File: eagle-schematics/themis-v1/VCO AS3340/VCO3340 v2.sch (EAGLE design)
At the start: 47 parts

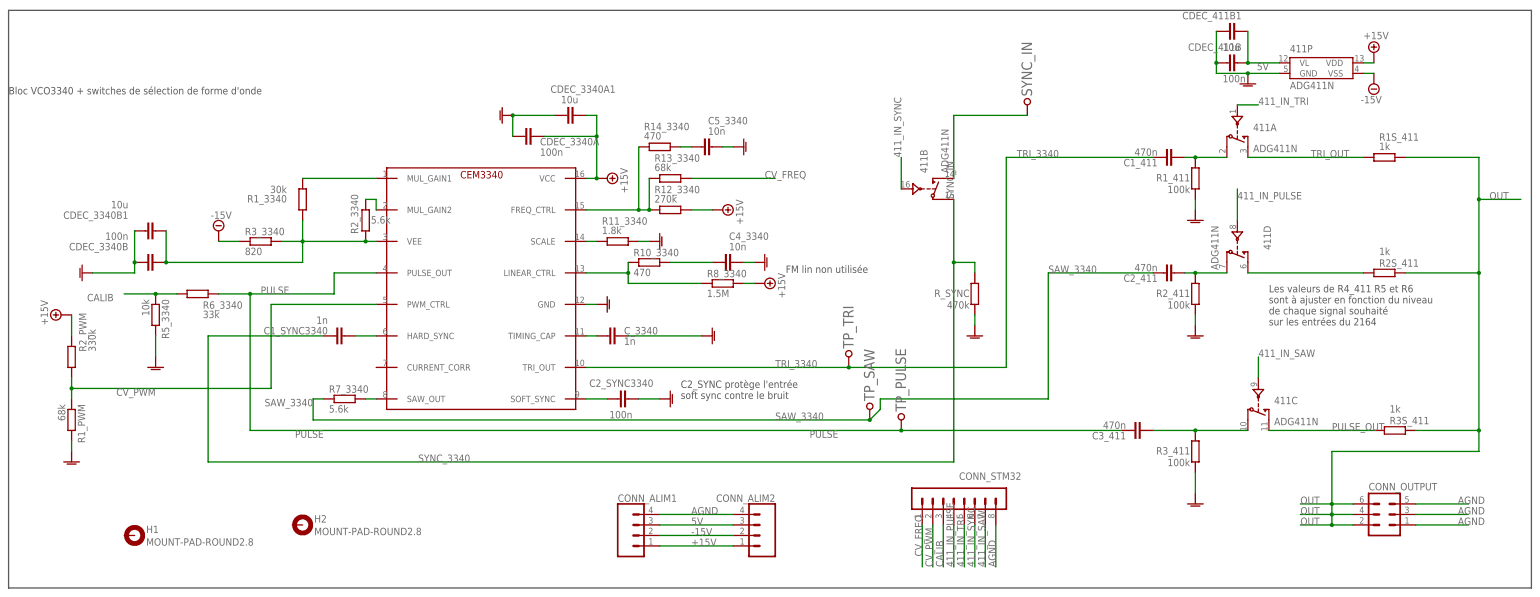
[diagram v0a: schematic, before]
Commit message: New version of DAC board based on AD5391 chip
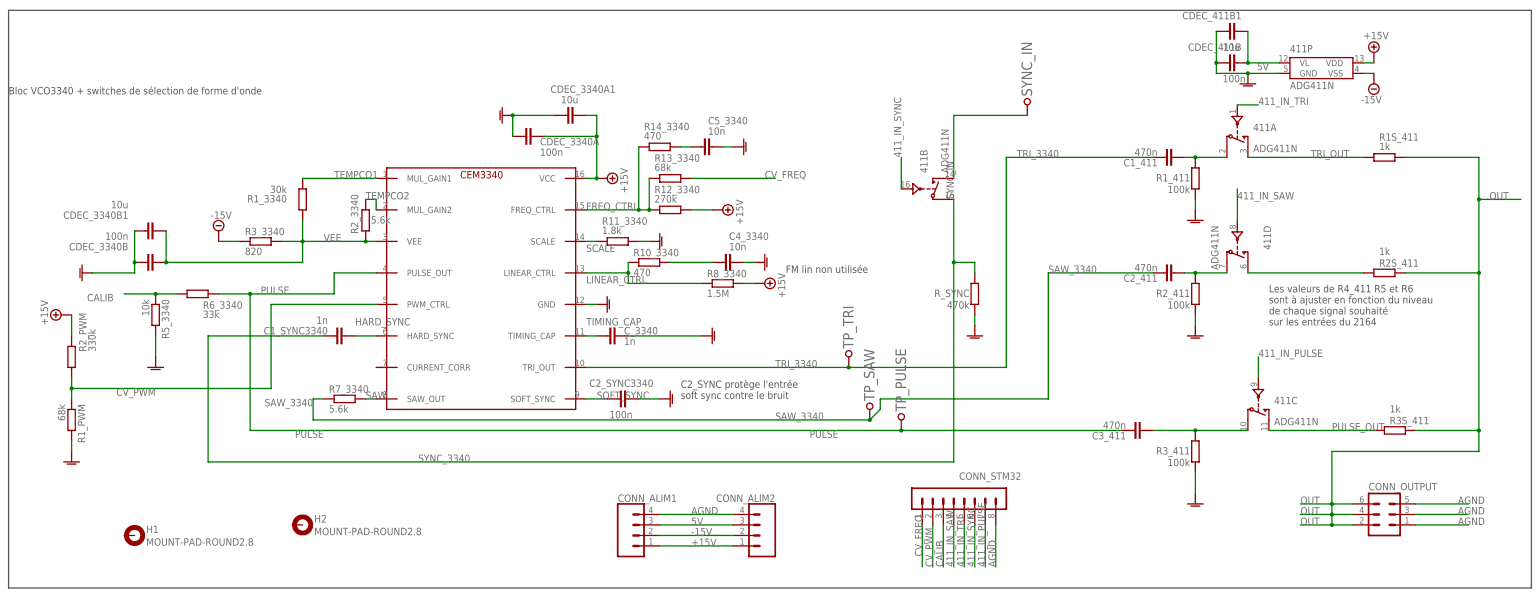
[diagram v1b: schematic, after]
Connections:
- net N$1 renamed SOFT_SYNC
- net N$16 renamed HARD_SYNC
- net N$2 renamed SAW_OUT
- net N$20 renamed TEMPCO1
- net N$23 renamed TEMPCO2
- net N$25 renamed LINEAR_CTRL
- net N$28 renamed SAW
- net N$30 renamed VEE
- net N$40 renamed FREQ_CTRL
- net N$43 renamed SCALE
- net N$46 renamed TIMING_CAP
- net N$49 renamed TRI_IN
- net N$50 renamed SAW_IN
- net N$51 renamed PULSE_IN
- net 411_IN_PULSE: now also 411C.IN, CONN_STM32.7; no longer 411D.IN, CONN_STM32.4
- net 411_IN_SAW: now also 411D.IN, CONN_STM32.4; no longer 411C.IN, CONN_STM32.7
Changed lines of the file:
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@@
 <?xml version="1.0" encoding="utf-8"?>
 <!DOCTYPE eagle SYSTEM "eagle.dtd">
-<eagle version="9.4.2">
+<eagle version="9.5.2">
 <drawing>
 <settings>
@@
 </segment>
 </net>
-<net name="N$20" class="0">
+<net name="TEMPCO1" class="0">
 <segment>
 <pinref part="CEM3340" gate="G$1" pin="MUL_GAIN1"/>
 <pinref part="R1_3340" gate="G$1" pin="1"/>
 <wire x1="-73.66" y1="-78.74" x2="-91.44" y2="-78.74" width="0.1524" layer="91"/>
-</segment>
-</net>
-<net name="N$23" class="0">
+<label x="-83.82" y="-78.74" size="1.778" layer="95"/>
+</segment>
+</net>
+<net name="TEMPCO2" class="0">
 <segment>
 <pinref part="CEM3340" gate="G$1" pin="MUL_GAIN2"/>
@@
 <wire x1="-73.66" y1="-86.36" x2="-73.66" y2="-83.82" width="0.1524" layer="91"/>
 <wire x1="-73.66" y1="-83.82" x2="-76.2" y2="-83.82" width="0.1524" layer="91"/>
-</segment>
-</net>
-<net name="N$28" class="0">
+<label x="-76.2" y="-83.82" size="1.778" layer="95"/>
+</segment>
+</net>
+<net name="SAW" class="0">
 <segment>
 <pinref part="CEM3340" gate="G$1" pin="SAW_OUT"/>
 <pinref part="R7_3340" gate="G$1" pin="2"/>
 <wire x1="-73.66" y1="-132.08" x2="-76.2" y2="-132.08" width="0.1524" layer="91"/>
-</segment>
-</net>
-<net name="N$30" class="0">
+<label x="-76.2" y="-132.08" size="1.778" layer="95"/>
+</segment>
+</net>
+<net name="VEE" class="0">
 <segment>
 <pinref part="CEM3340" gate="G$1" pin="VEE"/>
@@
 <junction x="-124.46" y="-99.06"/>
 <pinref part="CDEC_3340B1" gate="G$1" pin="2"/>
-</segment>
-</net>
-<net name="N$40" class="0">
+<label x="-86.36" y="-93.98" size="1.778" layer="95"/>
+</segment>
+</net>
+<net name="FREQ_CTRL" class="0">
 <segment>
 <pinref part="R14_3340" gate="G$1" pin="1"/>
@@
 <pinref part="R12_3340" gate="G$1" pin="1"/>
 <junction x="-7.62" y="-86.36"/>
+<label x="-22.86" y="-86.36" size="1.778" layer="95"/>
 </segment>
 </net>
@@
 </segment>
 </net>
-<net name="N$43" class="0">
+<net name="SCALE" class="0">
 <segment>
 <pinref part="CEM3340" gate="G$1" pin="SCALE"/>
 <pinref part="R11_3340" gate="G$1" pin="1"/>
 <wire x1="-22.86" y1="-93.98" x2="-20.32" y2="-93.98" width="0.1524" layer="91"/>
+<label x="-22.86" y="-96.52" size="1.778" layer="95"/>
 </segment>
 </net>
@@
 </segment>
 </net>
-<net name="N$46" class="0">
+<net name="TIMING_CAP" class="0">
 <segment>
 <pinref part="CEM3340" gate="G$1" pin="TIMING_CAP"/>
 <pinref part="C_3340" gate="G$1" pin="2"/>
 <wire x1="-22.86" y1="-116.84" x2="-20.32" y2="-116.84" width="0.1524" layer="91"/>
+<label x="-22.86" y="-114.3" size="1.778" layer="95"/>
 </segment>
 </net>
@@
 </segment>
 </net>
-<net name="N$25" class="0">
+<net name="LINEAR_CTRL" class="0">
 <segment>
 <pinref part="CEM3340" gate="G$1" pin="LINEAR_CTRL"/>
@@
 <wire x1="-12.7" y1="-99.06" x2="-12.7" y2="-101.6" width="0.1524" layer="91"/>
 <junction x="-12.7" y="-101.6"/>
+<label x="-22.86" y="-104.14" size="1.778" layer="95"/>
 </segment>
 </net>
@@
 </segment>
 </net>
-<net name="N$49" class="0">
+<net name="TRI_IN" class="0">
 <segment>
 <pinref part="411" gate="A" pin="D"/>
@@
 </segment>
 </net>
-<net name="N$50" class="0">
+<net name="SAW_IN" class="0">
 <segment>
 <pinref part="C2_411" gate="G$1" pin="2"/>
@@
 </segment>
 </net>
-<net name="N$51" class="0">
+<net name="PULSE_IN" class="0">
 <segment>
 <pinref part="411" gate="C" pin="D"/>
@@
 </segment>
 </net>
-<net name="N$1" class="0">
+<net name="SOFT_SYNC" class="0">
 <segment>
 <pinref part="C2_SYNC3340" gate="G$1" pin="2"/>
 <pinref part="CEM3340" gate="G$1" pin="SOFT_SYNC"/>
 <wire x1="-17.78" y1="-132.08" x2="-22.86" y2="-132.08" width="0.1524" layer="91"/>
-</segment>
-</net>
-<net name="N$16" class="0">
+<label x="-20.32" y="-132.08" size="1.778" layer="95"/>
+</segment>
+</net>
+<net name="HARD_SYNC" class="0">
 <segment>
 <pinref part="C1_SYNC3340" gate="G$1" pin="2"/>
 <pinref part="CEM3340" gate="G$1" pin="HARD_SYNC"/>
 <wire x1="-78.74" y1="-116.84" x2="-73.66" y2="-116.84" width="0.1524" layer="91"/>
+<label x="-78.74" y="-114.3" size="1.778" layer="95"/>
 </segment>
 </net>
@@
 </segment>
 </net>
-<net name="411_IN_PULSE" class="0">
+<net name="411_IN_SAW" class="0">
 <segment>
 <wire x1="134.62" y1="-88.9" x2="134.62" y2="-81.28" width="0.1524" layer="91"/>
@@
 </segment>
 </net>
-<net name="411_IN_SAW" class="0">
+<net name="411_IN_PULSE" class="0">
 <segment>
 <pinref part="CONN_STM32" gate="1" pin="7"/>
@@
 </segment>
 </net>
-<net name="N$2" class="0">
+<net name="SAW_OUT" class="0">
 <segment>
 <pinref part="411" gate="D" pin="S"/>
